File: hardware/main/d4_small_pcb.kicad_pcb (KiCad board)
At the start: 4 copper layers, 32 x 45 mm, 62 parts, among them J1 S2B-PH-SM4-TB_LF__SN_, J2 U_FL-R-SMT-1_10_, Q1 UMH3N, U1 BQ25180, U2 TTGO-Micro32-ESP32, U3 CAM-M8C, U4 RFM95W-868S2, U5 AP2112K-3.3, U6 CH340G, U7 RF430CL330HIRGTR‎, U8 BMA400

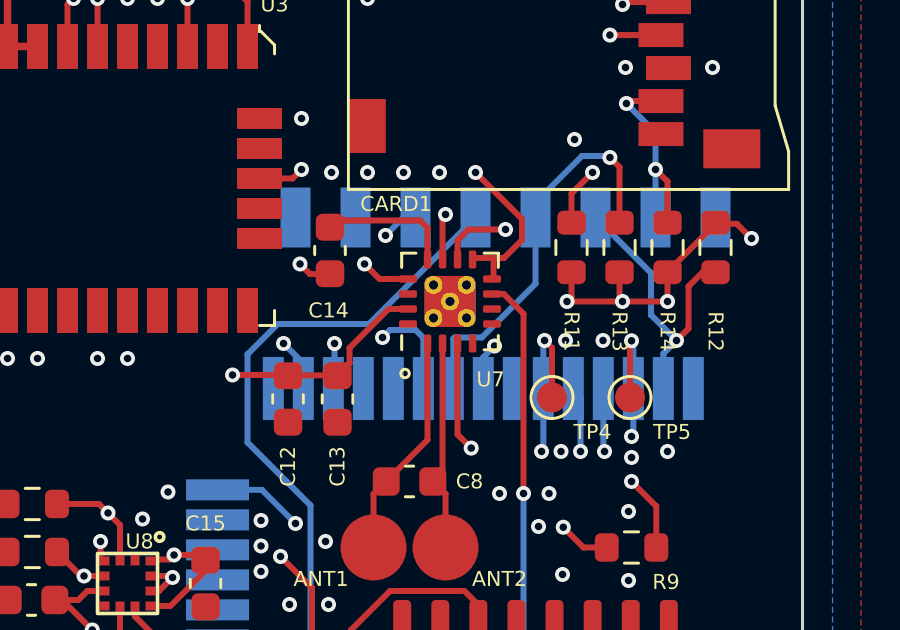
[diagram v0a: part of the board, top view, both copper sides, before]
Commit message: update RF430 footprint
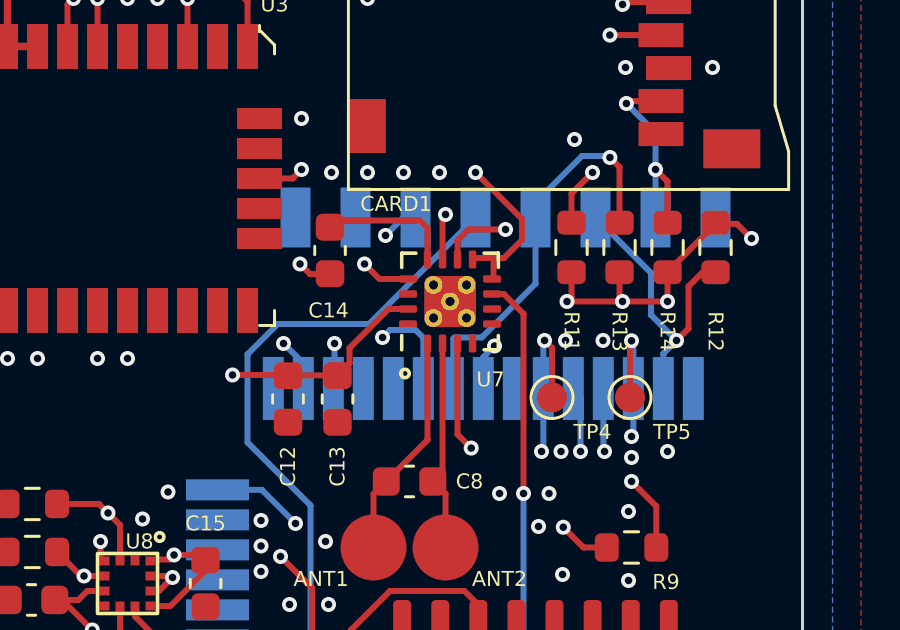
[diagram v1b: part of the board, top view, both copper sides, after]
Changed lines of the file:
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@@
 			(at 1.7 3.2)
 			(size 2.2 2.2)
-			(layers "F.Cu" "F.Paste" "F.Mask")
+			(layers "F.Cu" "F.Mask")
 			(net 1 "ANT1")
 			(pinfunction "1")
@@
 			(at 1.1 3.2)
 			(size 2.2 2.2)
-			(layers "F.Cu" "F.Paste" "F.Mask")
+			(layers "F.Cu" "F.Mask")
 			(net 2 "ANT2")
 			(pinfunction "1")
@@
 			)
 		)
-		(property "Description" ""
+		(property "Description" "RF RCVR GNSS/GPS 1.575GHZ MODULE"
 			(at -10.9 61.9 0)
 			(layer "F.Fab")
@@
 			(end 1.61 -1.135)
 			(stroke
-				(width 0.1)
+				(width 0.12)
 				(type solid)
 			)
@@
 			(end 1.61 -1.61)
 			(stroke
-				(width 0.1)
+				(width 0.12)
 				(type solid)
 			)
@@
 			(end -1.61 -1.61)
 			(stroke
-				(width 0.1)
+				(width 0.12)
 				(type solid)
 			)
@@
 			(end 1.61 1.135)
 			(stroke
-				(width 0.1)
+				(width 0.12)
 				(type solid)
 			)
@@
 			(end 1.61 1.61)
 			(stroke
-				(width 0.1)
+				(width 0.12)
 				(type solid)
 			)
@@
 			(end -1.61 1.61)
 			(stroke
-				(width 0.1)
+				(width 0.12)
 				(type solid)
 			)
@@
 			(end -1.61 1.135)
 			(stroke
-				(width 0.1)
+				(width 0.12)
 				(type solid)
 			)
@@
 			(end -2.5 -1.4)
 			(stroke
-				(width 0.1)
+				(width 0.12)
 				(type solid)
 			)
@@
 		)
 		(pad "3" smd roundrect
-			(at -1.4 0.25 90)
+			(at -1.4 0.25 270)
 			(size 0.6 0.25)
 			(layers "F.Cu" "F.Paste" "F.Mask")
@@
 		)
 		(pad "4" smd roundrect
-			(at -1.4 0.75 90)
+			(at -1.4 0.75 270)
 			(size 0.6 0.25)
 			(layers "F.Cu" "F.Paste" "F.Mask")
@@
 		)
 		(pad "5" smd roundrect
-			(at -0.75 1.4 90)
-			(size 0.25 0.6)
+			(at -0.75 1.4 180)
+			(size 0.6 0.25)
 			(layers "F.Cu" "F.Paste" "F.Mask")
 			(roundrect_rratio 0.25)
@@
 		)
 		(pad "6" smd roundrect
-			(at -0.25 1.4 90)
-			(size 0.25 0.6)
+			(at -0.25 1.4 180)
+			(size 0.6 0.25)
 			(layers "F.Cu" "F.Paste" "F.Mask")
 			(roundrect_rratio 0.25)
@@
 		)
 		(pad "7" smd roundrect
-			(at 0.25 1.4 90)
-			(size 0.25 0.6)
+			(at 0.25 1.4 180)
+			(size 0.6 0.25)
 			(layers "F.Cu" "F.Paste" "F.Mask")
 			(roundrect_rratio 0.25)
@@
 		)
 		(pad "8" smd roundrect
-			(at 0.75 1.4 90)
-			(size 0.25 0.6)
+			(at 0.75 1.4 180)
+			(size 0.6 0.25)
 			(layers "F.Cu" "F.Paste" "F.Mask")
 			(roundrect_rratio 0.25)
@@
 		)
 		(pad "9" smd roundrect
-			(at 1.4 0.75 90)
+			(at 1.4 0.75 270)
 			(size 0.6 0.25)
 			(layers "F.Cu" "F.Paste" "F.Mask")
@@
 		)
 		(pad "10" smd roundrect
-			(at 1.4 0.25 90)
+			(at 1.4 0.25 270)
 			(size 0.6 0.25)
 			(layers "F.Cu" "F.Paste" "F.Mask")
@@
 		)
 		(pad "11" smd roundrect
-			(at 1.4 -0.25 90)
+			(at 1.4 -0.25 270)
 			(size 0.6 0.25)
 			(layers "F.Cu" "F.Paste" "F.Mask")
@@
 		)
 		(pad "12" smd roundrect
-			(at 1.4 -0.75 90)
+			(at 1.4 -0.75 270)
 			(size 0.6 0.25)
 			(layers "F.Cu" "F.Paste" "F.Mask")
@@
 		)
 		(pad "13" smd roundrect
-			(at 0.75 -1.4 90)
-			(size 0.25 0.6)
+			(at 0.75 -1.4)
+			(size 0.6 0.25)
 			(layers "F.Cu" "F.Paste" "F.Mask")
 			(roundrect_rratio 0.25)
@@
 		)
 		(pad "14" smd roundrect
-			(at 0.25 -1.4 90)
-			(size 0.25 0.6)
+			(at 0.25 -1.4)
+			(size 0.6 0.25)
 			(layers "F.Cu" "F.Paste" "F.Mask")
 			(roundrect_rratio 0.25)
@@
 		)
 		(pad "15" smd roundrect
-			(at -0.25 -1.4 90)
-			(size 0.25 0.6)
+			(at -0.25 -1.4)
+			(size 0.6 0.25)
 			(layers "F.Cu" "F.Paste" "F.Mask")
 			(roundrect_rratio 0.25)
@@
 		)
 		(pad "16" smd roundrect
-			(at -0.75 -1.4 90)
-			(size 0.25 0.6)
+			(at -0.75 -1.4)
+			(size 0.6 0.25)
 			(layers "F.Cu" "F.Paste" "F.Mask")
 			(roundrect_rratio 0.25)
@@
 			(layers "*.Cu")
 			(remove_unused_layers no)
-			(net 72 "unconnected-(U7-PAD-Pad17)_1")
+			(net 77 "unconnected-(U7-PAD-Pad17)_3")
 			(pinfunction "PAD")
 			(pintype "no_connect")
@@
 			(layers "*.Cu")
 			(remove_unused_layers no)
-			(net 76 "unconnected-(U7-PAD-Pad17)_2")
+			(net 71 "unconnected-(U7-PAD-Pad17)")
 			(pinfunction "PAD")
 			(pintype "no_connect")
@@
 			(layers "*.Cu")
 			(remove_unused_layers no)
-			(net 91 "unconnected-(U7-PAD-Pad17)_6")
+			(net 76 "unconnected-(U7-PAD-Pad17)_2")
 			(pinfunction "PAD")
 			(pintype "no_connect")
@@
 			(layers "F.Cu" "F.Mask")
 			(roundrect_rratio 0.147059)
-			(net 71 "unconnected-(U7-PAD-Pad17)")
+			(net 72 "unconnected-(U7-PAD-Pad17)_1")
 			(pinfunction "PAD")
 			(pintype "no_connect")
@@
 			(layers "B.Cu")
 			(roundrect_rratio 0.147059)
-			(net 77 "unconnected-(U7-PAD-Pad17)_3")
+			(net 91 "unconnected-(U7-PAD-Pad17)_6")
 			(pinfunction "PAD")
 			(pintype "no_connect")
@@
 			(layers "*.Cu")
 			(remove_unused_layers no)
-			(net 89 "unconnected-(U7-PAD-Pad17)_5")
+			(net 85 "unconnected-(U7-PAD-Pad17)_4")
 			(pinfunction "PAD")
 			(pintype "no_connect")
@@
 			(layers "*.Cu")
 			(remove_unused_layers no)
-			(net 85 "unconnected-(U7-PAD-Pad17)_4")
+			(net 89 "unconnected-(U7-PAD-Pad17)_5")
 			(pinfunction "PAD")
 			(pintype "no_connect")
@@
 			)
 		)
-		(property "Description" ""
+		(property "Description" "CONN HEADER SMD R/A 2POS 2MM"
 			(at 48.6 118.7 0)
 			(layer "F.Fab")
@@
 			)
 		)
-		(property "Description" ""
+		(property "Description" "CONN U.FL RCPT STR 50 OHM SMD"
 			(at 3.26 48.66 0)
 			(layer "F.Fab")
